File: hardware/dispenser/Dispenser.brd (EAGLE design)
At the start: 73.7 x 75.6 mm, 65 parts, among them J1 AVR_Prog, J2 RJ45-8PTH, Q1 NFET-SO8, Q2 NFET, Q3 NFET, Q4 NFET, Q5 MOSFET-NCHANNELSMD, U1 ATMEGA168, U10 HALL-EFFECT, U2 OPAMP-DUAL, U3 OPTO-TLP185, U4 MPX10DP, U5 VREG-5V-LDO-AP1117SOT89-3L, U6 WS2801, U7 HALL-EFFECT, U8 HALL-EFFECT, U9 HALL-EFFECT

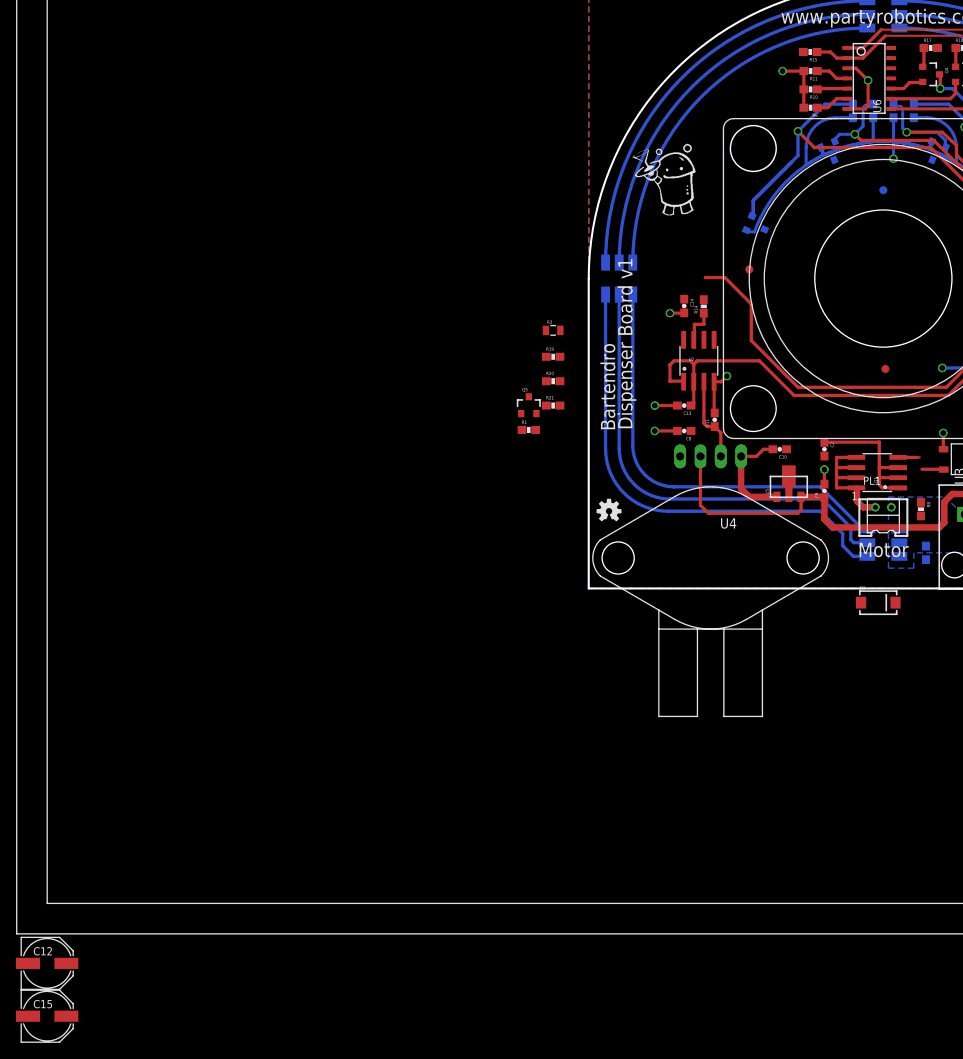
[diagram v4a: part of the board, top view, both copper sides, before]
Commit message: removed LED_DATA pull up
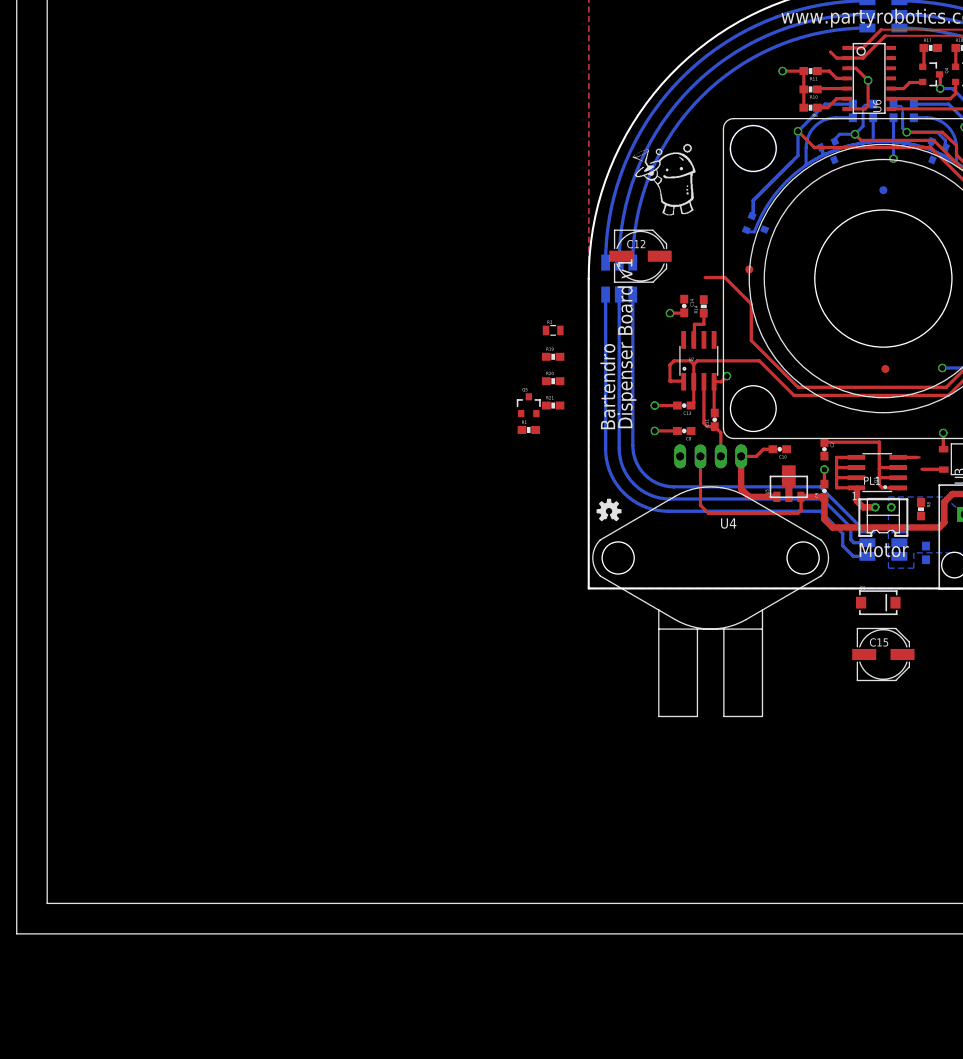
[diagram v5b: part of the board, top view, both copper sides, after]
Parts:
- removed R15: 1k, SparkFun-Resistors:0603-RES
- moved C12 115.4 mm to (6.48, 41.5)
- moved C15 113.9 mm to (36.8, -8.26)
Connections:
- net 3.3V: no longer R15.2
- net LED_DATA: no longer R15.1
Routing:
- net LED_DATA: track 64.5 -> 62.8 mm
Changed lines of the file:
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@@
 <element name="R13" library="SparkFun-Resistors" package="0603-RES" value="10k" x="33.02" y="59.69" rot="MR270"/>
 <element name="U6" library="SparkFun-DigitalIC" package="SOP-14" value="WS2801" x="35.052" y="63.754" rot="R270"/>
-<element name="R15" library="SparkFun-Resistors" package="0603-RES" value="1k" x="27.686" y="67.056" rot="R180"/>
 <element name="C11" library="SparkFun" package="0603-CAP" value="100n" x="15.748" y="21.082" rot="R90"/>
 <element name="R16" library="SparkFun-Resistors" package="0603-RES" value="10k" x="51.054" y="67.564"/>
@@
 <attribute name="PROD_ID" value="DIO-09886" x="36.195" y="-1.778" size="1.778" layer="27" display="off"/>
 </element>
-<element name="C12" library="SparkFun-Capacitors" package="PANASONIC_D" value="100u 6.3V" x="-67.691" y="-46.863"/>
-<element name="C15" library="SparkFun-Capacitors" package="PANASONIC_D" value="47u 35V" x="-67.691" y="-53.467"/>
+<element name="C12" library="SparkFun-Capacitors" package="PANASONIC_D" value="100u 6.3V" x="6.477" y="41.529"/>
+<element name="C15" library="SparkFun-Capacitors" package="PANASONIC_D" value="47u 35V" x="36.83" y="-8.255"/>
 </elements>
 <signals>
@@
 <contactref element="Q5" pad="2"/>
 <contactref element="C12" pad="-"/>
-<wire x1="-6.543" y1="21.86" x2="-70.091" y2="-46.863" width="0" layer="19" extent="1-1"/>
+<wire x1="-6.543" y1="21.86" x2="4.077" y2="41.529" width="0" layer="19" extent="1-1"/>
 <wire x1="-3.595" y1="25.908" x2="-6.543" y2="21.86" width="0" layer="19" extent="1-1"/>
 <wire x1="-5.345" y1="32.258" x2="-3.595" y2="25.908" width="0" layer="19" extent="1-1"/>
@@
 <wire x1="52.959" y1="44.577" x2="52.9336" y2="44.6024" width="0.254" layer="16"/>
 <contactref element="U6" pad="14"/>
-<contactref element="R15" pad="2"/>
 <contactref element="R17" pad="2"/>
 <contactref element="R18" pad="2"/>
@@
 <wire x1="37.802" y1="67.564" x2="43.5982" y2="67.564" width="0" layer="19" extent="1-1"/>
 <wire x1="38.1" y1="58.84" x2="37.802" y2="67.564" width="0" layer="19" extent="1-16"/>
-<wire x1="26.836" y1="67.056" x2="30.9" y2="58.84" width="0" layer="19" extent="1-16"/>
 <wire x1="52.2732" y1="46.1518" x2="45.974" y2="53.213" width="0" layer="19" extent="16-16"/>
 <wire x1="57.7088" y1="43.981" x2="52.959" y2="43.434" width="0" layer="19" extent="1-16"/>
@@
 <contactref element="U1" pad="2"/>
 <contactref element="U6" pad="2"/>
-<contactref element="R15" pad="1"/>
 <wire x1="32.302" y1="66.294" x2="30.988" y2="66.294" width="0.4064" layer="1"/>
 <wire x1="30.988" y1="66.294" x2="30.226" y2="67.056" width="0.4064" layer="1"/>
-<wire x1="30.226" y1="67.056" x2="28.536" y2="67.056" width="0.4064" layer="1"/>
 <wire x1="32.302" y1="66.294" x2="34.29" y2="66.294" width="0.4064" layer="1"/>
 <wire x1="34.29" y1="66.294" x2="37.084" y2="69.088" width="0.4064" layer="1"/>
@@
 <wire x1="58.3504" y1="38.7924" x2="60.2234" y2="38.7924" width="0.4064" layer="1"/>
 <contactref element="C12" pad="+"/>
-<wire x1="14.3764" y1="36.1052" x2="-65.291" y2="-46.863" width="0" layer="19" extent="1-1"/>
+<wire x1="14.3764" y1="36.1052" x2="8.877" y2="41.529" width="0" layer="19" extent="1-1"/>
 <wire x1="14.5572" y1="38.862" x2="14.4048" y2="36.1336" width="0" layer="19" extent="1-1"/>
 </signal>
@@
 <contactref element="D1" pad="C"/>
 <contactref element="C15" pad="+"/>
-<wire x1="38.345" y1="-1.778" x2="-65.291" y2="-53.467" width="0" layer="19" extent="1-1"/>
+<wire x1="38.345" y1="-1.778" x2="39.23" y2="-8.255" width="0" layer="19" extent="1-1"/>
 <wire x1="38.83" y1="4.015" x2="38.345" y2="-1.778" width="0" layer="19" extent="1-16"/>
 <wire x1="38.83" y1="5.715" x2="38.83" y2="4.015" width="0" layer="19" extent="16-16"/>

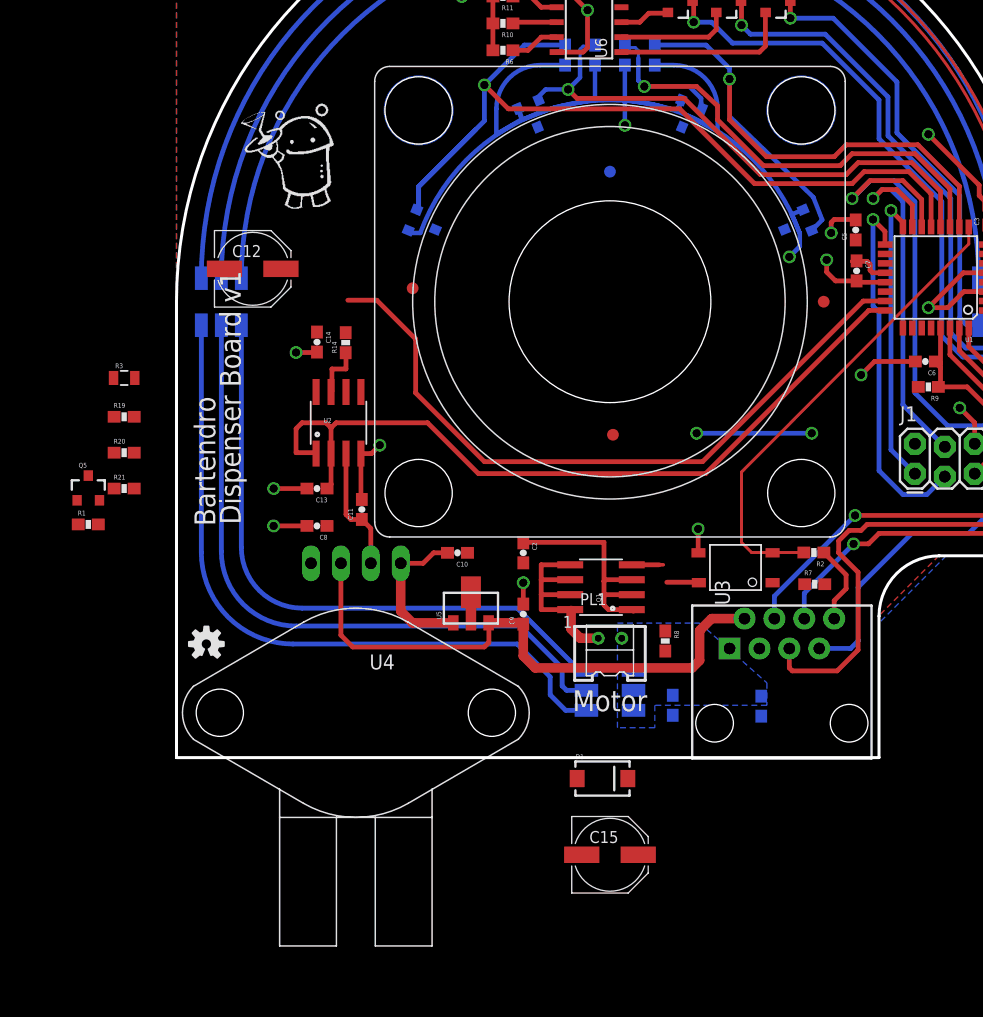
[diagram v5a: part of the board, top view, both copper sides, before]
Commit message: Finished Dispenser Layout!
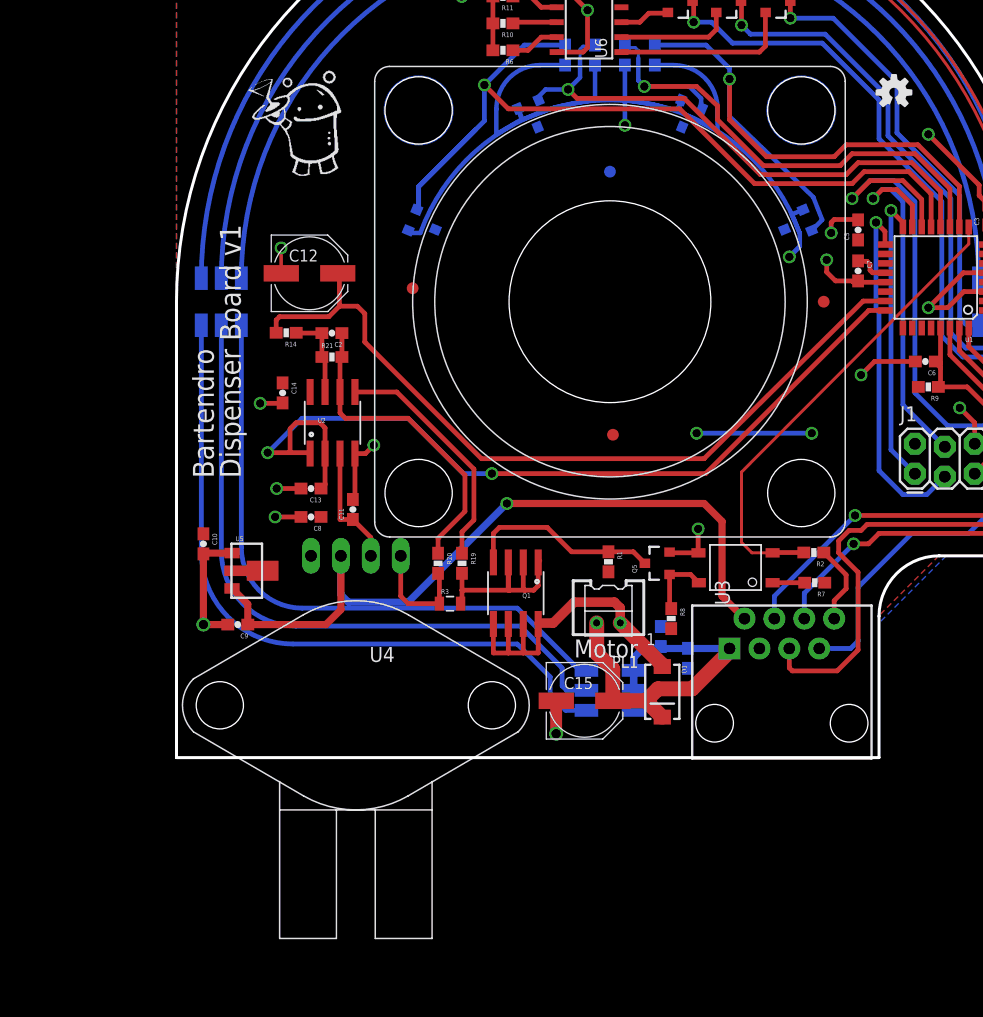
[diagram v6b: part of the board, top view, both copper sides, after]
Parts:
- PL1: value Motor Connector -> (none)
- moved U$4 74.9 mm to (61.0, 56.5)
- moved Q5 48.8 mm to (40.9, 16.5), turned to 90 degrees
- moved R1 44.3 mm to (36.7, 16.6), turned to 270 degrees
- moved R3 33.7 mm to (23.2, 13.1)
- moved R19 31.3 mm to (24.3, 16.5), turned to 270 degrees
- moved R20 28.3 mm to (22.2, 16.5), turned to 270 degrees
- moved C2 24.8 mm to (13.2, 36.1), turned to 180 degrees
- moved C9 24.3 mm to (5.21, 11.3), turned to 180 degrees
- moved C10 21.6 mm to (2.29, 18.2), turned to 270 degrees
- moved R21 20.9 mm to (13.2, 34.0)
- moved U5 19.3 mm to (5.97, 15.9), turned to 270 degrees
- moved C15 13.3 mm to (34.7, 4.83)
- moved D1 8.95 mm to (41.3, 5.59), turned to 270 degrees
- moved C4 7.43 mm to (43.5, 8.43)
- moved Q1 7.26 mm to (28.8, 14.0), turned to 180 degrees
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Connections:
- removed net N$15: C15.-
- net GND: now also C15.-
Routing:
- net VIN: track 0.00 -> 37.7 mm
- net N$10: track 0.00 -> 27.3 mm
- net N$11: track 0.00 -> 20.4 mm
- net 5V: track 49.1 -> 65.7 mm, vias 0 -> 1
- net N$9: track 2.68 -> 16.8 mm
- net GND: track 92.2 -> 103.9 mm, vias 14 -> 16
- net MOT_B: track 18.0 -> 28.1 mm
- net CUR_SEN: track 59.7 -> 69.4 mm
- net LIQ_LVL: track 67.2 -> 75.7 mm, vias 0 -> 2
- net N$31: track 2.92 -> 5.74 mm
- net MOT_CUR: track 4.58 -> 7.31 mm
- net N$16: track 0.00 -> 2.73 mm
- net 1/4W: track 19.8 -> 18.5 mm
- net N$1: track 3.83 -> 3.03 mm
- net SCK: track 31.2 -> 30.4 mm
- removed copper zone on layer 16, net VIN

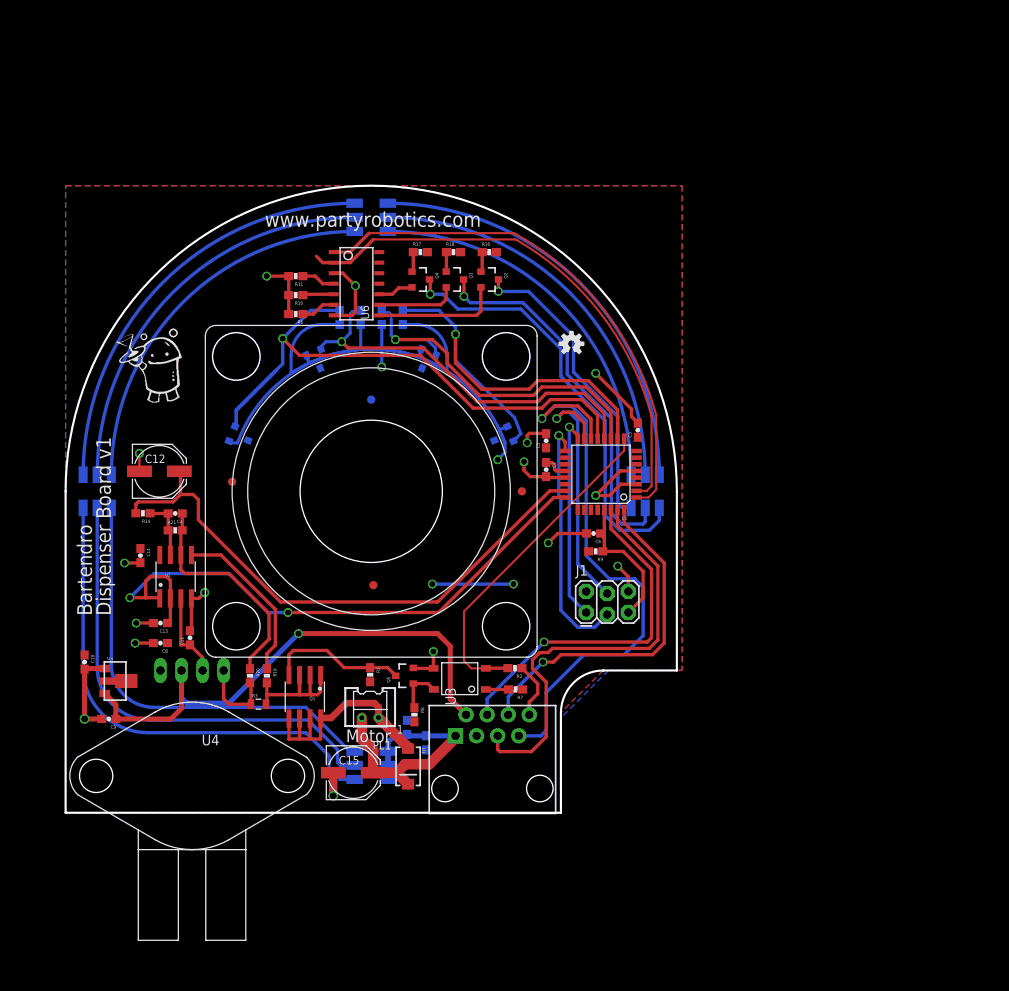
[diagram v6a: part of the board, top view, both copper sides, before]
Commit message: cleaned up dispenser layout silkscreen and design rules.
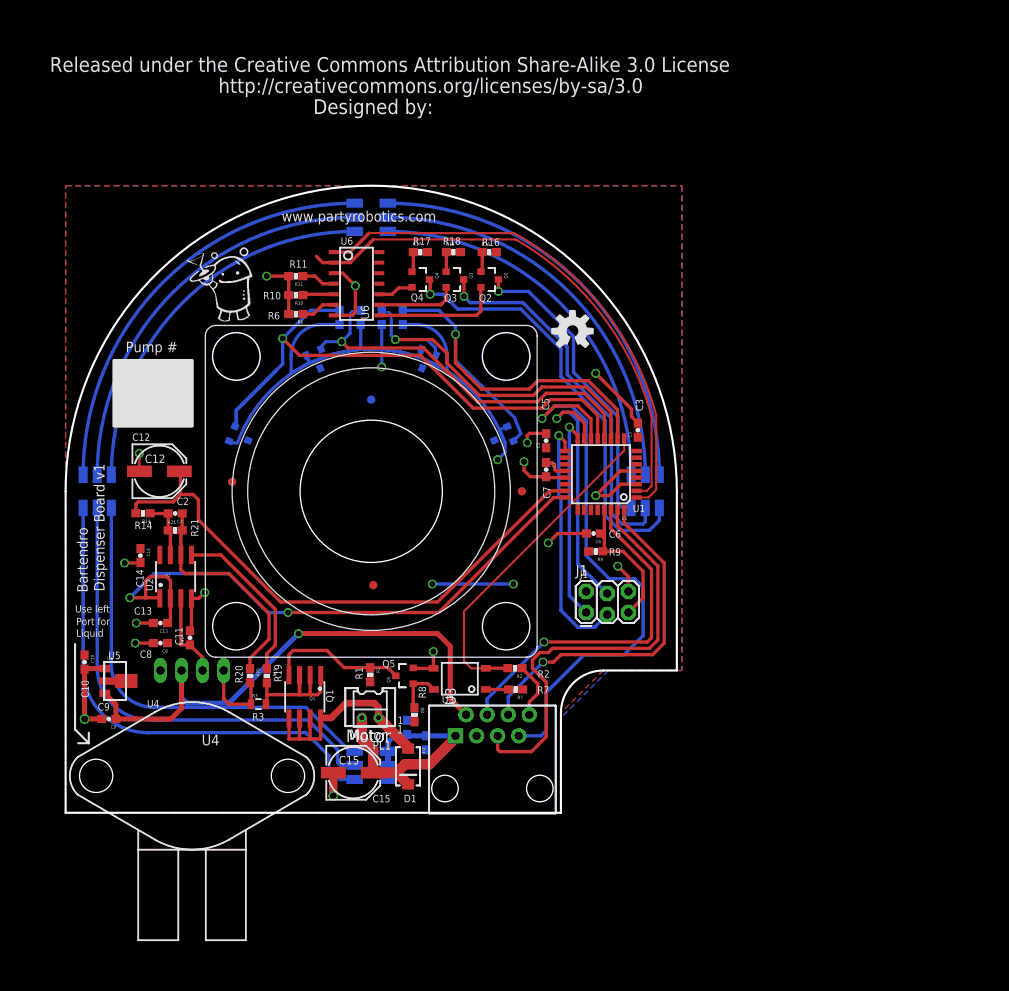
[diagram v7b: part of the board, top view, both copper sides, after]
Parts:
- removed U$4: OSHW-LOGOS, SparkFun-Aesthetics:OSHW-LOGO-S
- added U$1: OSHW-LOGOM, pierre:OSHW-LOGO-M
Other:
- board text added: "1"
- board text added: "C1"
- board text added: "C10"
- board text added: "C11"
- board text added: "C12"
- board text added: "C13"
- board text added: "C14"
- board text added: "C15"
- board text added: "C2"
- board text added: "C3"
- board text added: "C4"
- board text added: "C5"
- board text added: "C6"
- board text added: "C7"
- board text added: "C8"
- board text added: "C9"
- board text added: "D1"
- board text added: "Designed by:"
- board text added: "J1"
- board text added: "LED1"
- board text added: "LED2"
- board text added: "LED3"
- board text added: "LED4"
- board text added: "Liquid"
- board text added: "Port for"
- board text added: "Pump #"
- board text added: "Q1"
- board text added: "Q2"
- board text added: "Q3"
- board text added: "Q4"
- board text added: "Q5"
- board text added: "R1"
- board text added: "R10"
- board text added: "R11"
- board text added: "R12"
- board text added: "R13"
- board text added: "R14"
- board text added: "R16"
- board text added: "R17"
- board text added: "R18"
- board text added: "R19"
- board text added: "R2"
- board text added: "R20"
- board text added: "R21"
- board text added: "R3"
- board text added: "R4"
- board text added: "R5"
- board text added: "R6"
- board text added: "R7"
- board text added: "R8"
- board text added: "R9"
- board text added: "Released under the Creative Commons Attribution Share-Alike 3.0 License"
- board text added: "U1"
- board text added: "U10"
- board text added: "U2"
- board text added: "U3"
- board text added: "U4"
- board text added: "U5"
- board text added: "U6"
- board text added: "U7"
- board text added: "U8"
- board text added: "U9"
- board text added: "Use left"
- board text added: "http://creativecommons.org/licenses/by-sa/3.0"
